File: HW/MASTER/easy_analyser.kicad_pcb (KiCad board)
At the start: 2 copper layers, 49 x 33 mm, 65 parts, among them J1 USB-C_GCT_USB4105-GF-A, J2 header_02x10_male, J3 header_01x02_male, U1 IP425x-8, U2 IP425x-8, U3 CY7C68013A, U4 MIC5317, U5 24LC01, Y1 24MHz

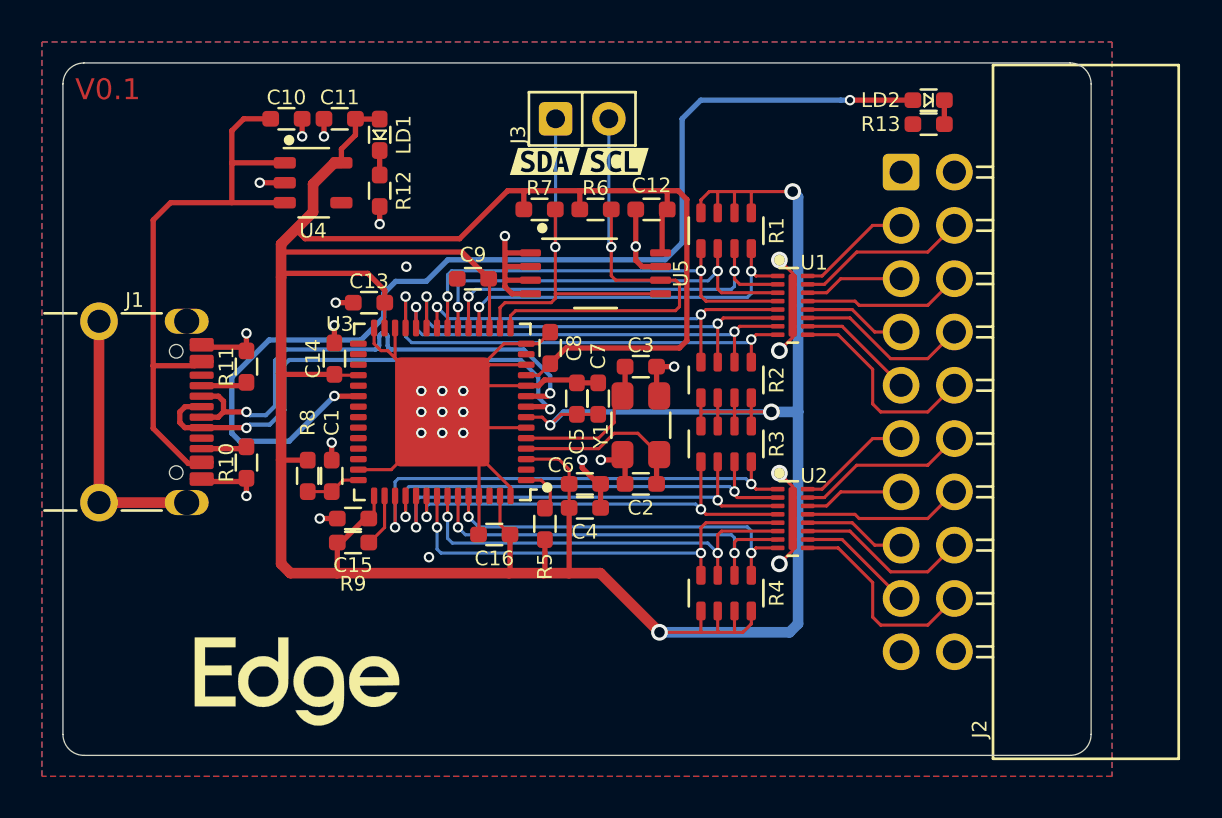
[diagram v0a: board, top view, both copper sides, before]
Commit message: Made changes for better fabrication (0.125mm tracks)
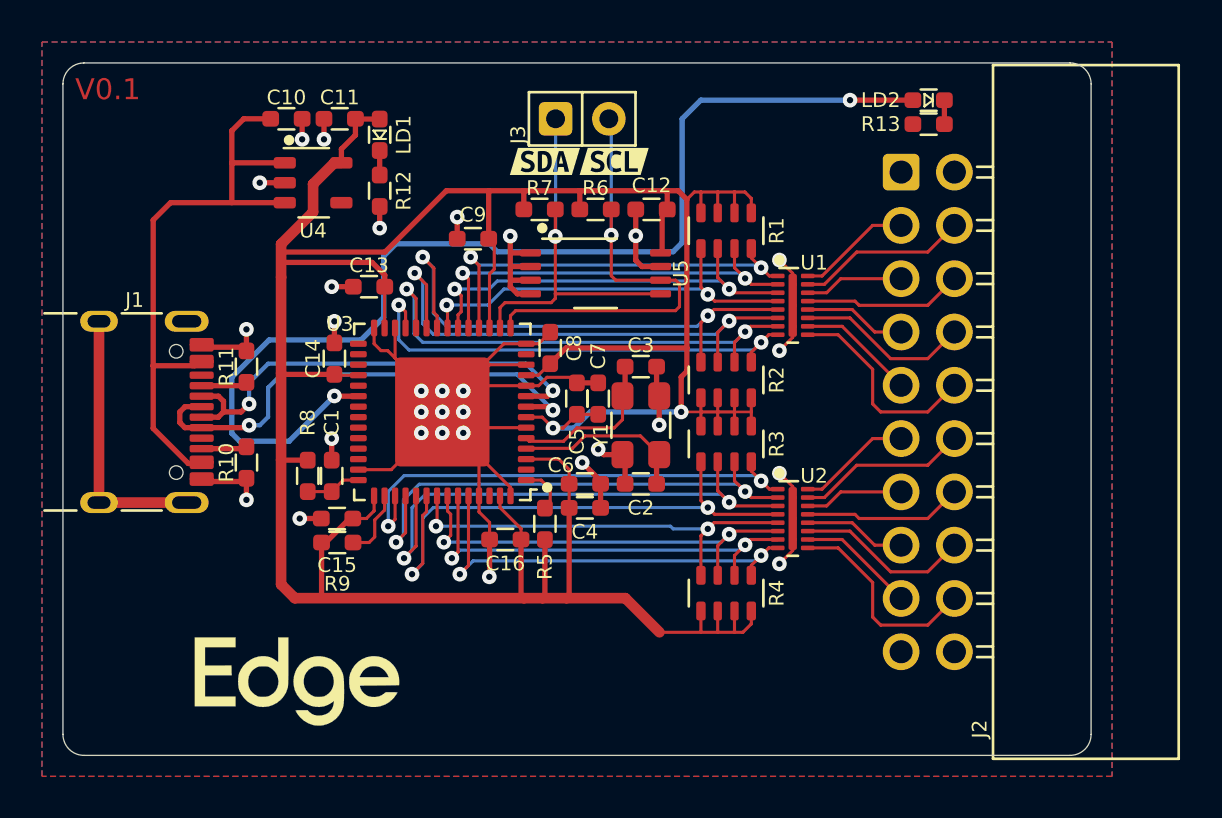
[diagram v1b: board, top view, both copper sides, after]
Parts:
- moved C9 1.91 mm to (129.5, 95.4)
- moved C13 0.76 mm to (124.6, 97.7)
- moved C15 0.76 mm to (123.1, 108.7)
- moved R9 0.75 mm to (123.1, 109.9)
- moved C16 0.58 mm to (131.1, 109.7)
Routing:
- net +3V3: track 195.0 -> 166.2 mm, vias 4 -> 2
- net /PB4: track 19.9 -> 25.9 mm
- net /PD3: track 20.8 -> 26.5 mm
- net GND: track 89.6 -> 94.1 mm
- net /PD2: track 22.1 -> 25.9 mm
- net /PB5: track 21.5 -> 25.1 mm
- net /USB_N: track 24.8 -> 22.0 mm
- net /PB6: track 21.0 -> 23.8 mm
- net /PD1: track 21.8 -> 24.6 mm
- net /PD7: track 18.2 -> 20.7 mm
- net /PB0: track 17.7 -> 19.7 mm
- net /PA1: track 51.8 -> 53.2 mm
- net /PD6: track 19.3 -> 20.7 mm
- net /USB_P: track 24.7 -> 23.5 mm
- net /PB3: track 20.7 -> 19.8 mm
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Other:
- net class Default: clearance 0.15 -> 0.125; trace_width 0.15 -> 0.125; via_dia 0.5 -> 0.7
- rule trace_clearance: 0.15 -> 0.125
- rule trace_min: 0.15 -> 0.125
- rule via_min_size: 0.5 -> 0.7

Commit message: Updated all tracks to be at least 0.15mm, made vias 0.7mm with a 0.3mm drill and added teardrops
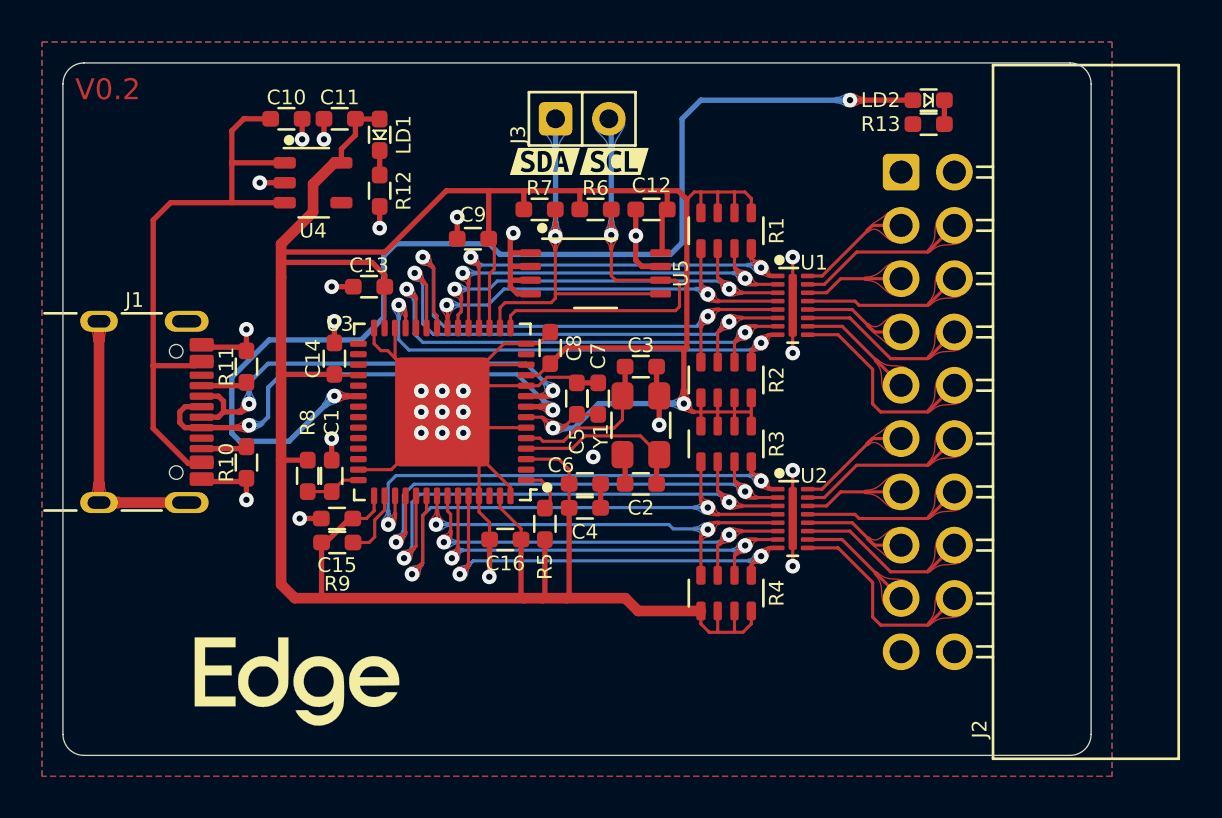
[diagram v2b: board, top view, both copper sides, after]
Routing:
- net GND: track 94.1 -> 91.1 mm, vias 30 -> 29
- net +3V3: track 166.2 -> 165.4 mm
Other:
- net class Default: clearance 0.125 -> 0.15; trace_width 0.125 -> 0.15
- rule trace_clearance: 0.125 -> 0.15
- rule trace_min: 0.125 -> 0.15
- board text added: "V0.2"
- board text removed: "V0.1"
